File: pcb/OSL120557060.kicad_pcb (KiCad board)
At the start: 2 copper layers, 115.6 x 105.4 mm, 79 parts, among them J1 USB_B_Micro, J2 USB_B_Micro, J3 AVR-ISP-6, SW1 SW_SPST, SW10 SW_SPST, SW11 SW_SPST, SW12 SW_SPST, SW13 SW_SPST, SW14 SW_SPST, SW15 SW_SPST, SW16 SW_SPST, SW17 SW_SPST, SW18 SW_SPST, SW19 SW_SPST, SW2 SW_SPST, SW20 SW_SPST, SW21 SW_SPST, SW22 SW_SPST, SW23 SW_SPST, SW24 SW_SPST, SW25 SW_SPST, SW26 SW_SPST, SW27 SW_SPST, SW28 SW_SPST, SW29 SW_SPST, SW3 SW_SPST, SW30 SW_SPST, SW4 SW_SPST, SW5 SW_SPST, SW6 SW_SPST, SW7 SW_SPST, SW8 SW_SPST, SW9 SW_SPST, U1 ATmega328-PU, X1 16MHz

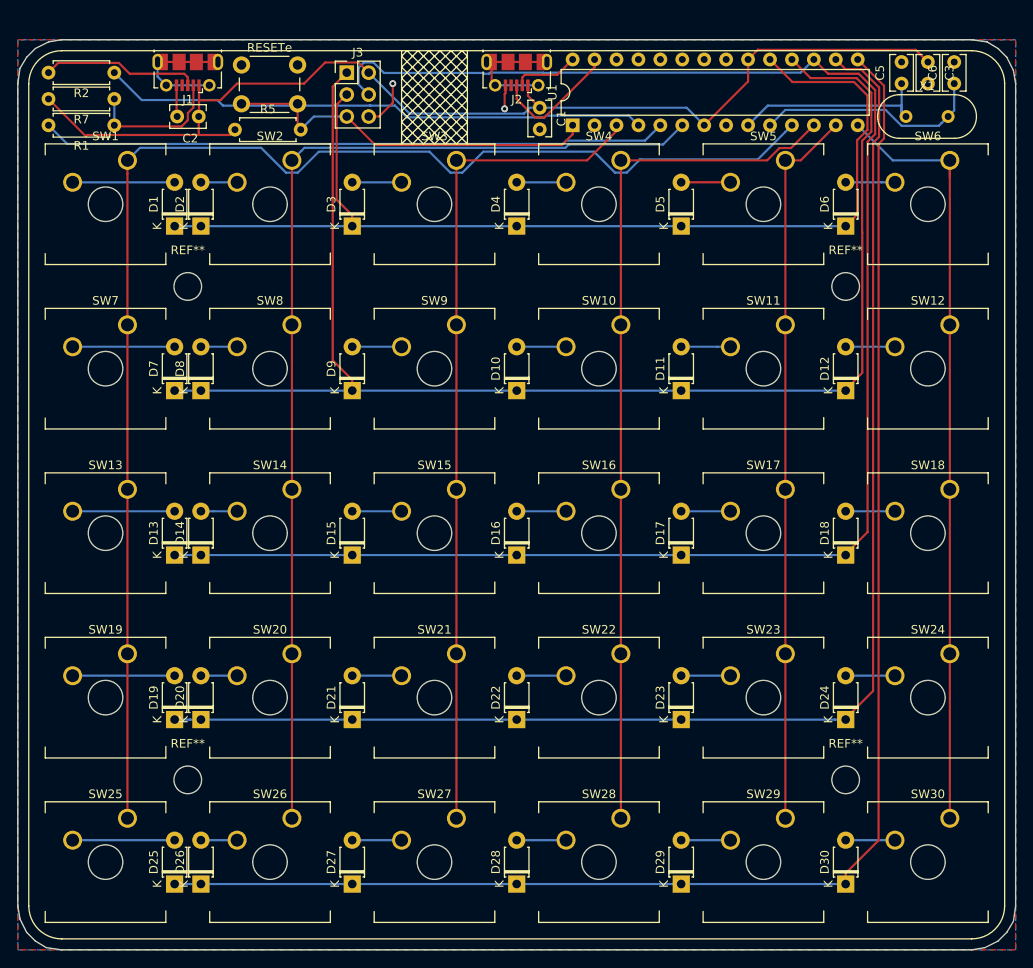
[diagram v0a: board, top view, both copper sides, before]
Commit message: added missing reset switch
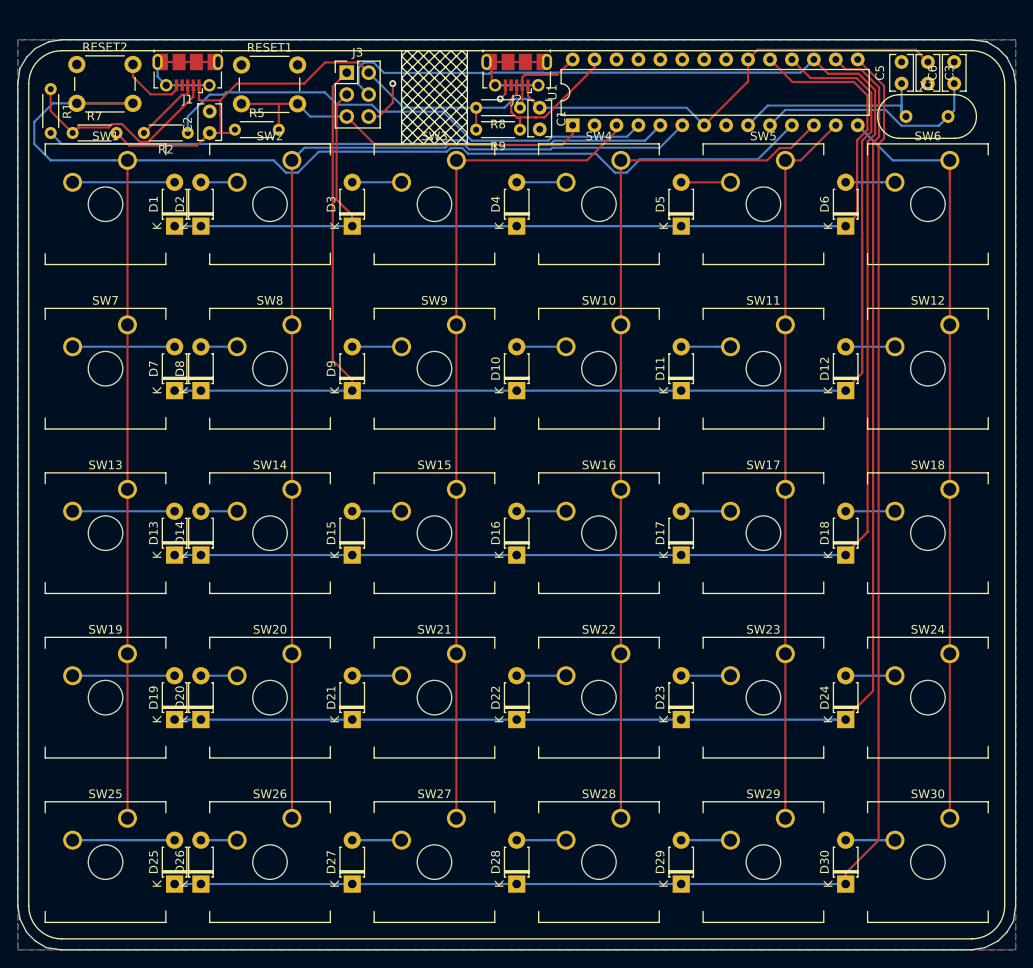
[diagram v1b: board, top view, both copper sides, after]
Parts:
- removed REF** (x4): MountingHole_3.2mm_M3, MountingHole:MountingHole_3.2mm_M3
- added R8: 10k, Resistor_THT:R_Axial_DIN0204_L3.6mm_D1.6mm_P5.08mm_Horizontal, F.Cu at (106.4, 58.7)
- added R9: 10k, Resistor_THT:R_Axial_DIN0204_L3.6mm_D1.6mm_P5.08mm_Horizontal, F.Cu at (106.4, 61.2)
- added RESET2: SW_SPST, Button_Switch_THT:SW_PUSH_6mm_H4.3mm, F.Cu at (55.1, 53.7)
- R1, R2, R5, R7: footprint Resistor_THT:R_Axial_DIN0207_L6.3mm_D2.5mm_P7.62mm_Horizontal -> Resistor_THT:R_Axial_DIN0204_L3.6mm_D1.6mm_P5.08mm_Horizontal
- moved R2 11.0 mm to (67.9, 61.6)
- moved R1 8.47 mm to (52.1, 56.5), turned to 270 degrees
- moved R7 6.23 mm to (54.6, 61.6), turned to 0 degrees
- moved C2 2.29 mm to (70.5, 61.6), turned to 90 degrees
- renumbered RESETe to RESET1
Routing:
- net /Col1: track 161.3 -> 191.3 mm
- net Net-(J1-Pad3): track 18.2 -> 8.00 mm
- net Net-(J1-Pad2): track 16.4 -> 24.9 mm
- net +5V: track 128.1 -> 122.1 mm
- net /USB_D+: track 63.5 -> 58.4 mm
- net GND: track 12.1 -> 15.5 mm
- net /SDA: track 14.8 -> 18.2 mm
- net /SCL: track 7.61 -> 10.3 mm
- net /Col2: track 123.1 -> 123.6 mm

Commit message: added smaller reset switches moved components to allow for all around plate
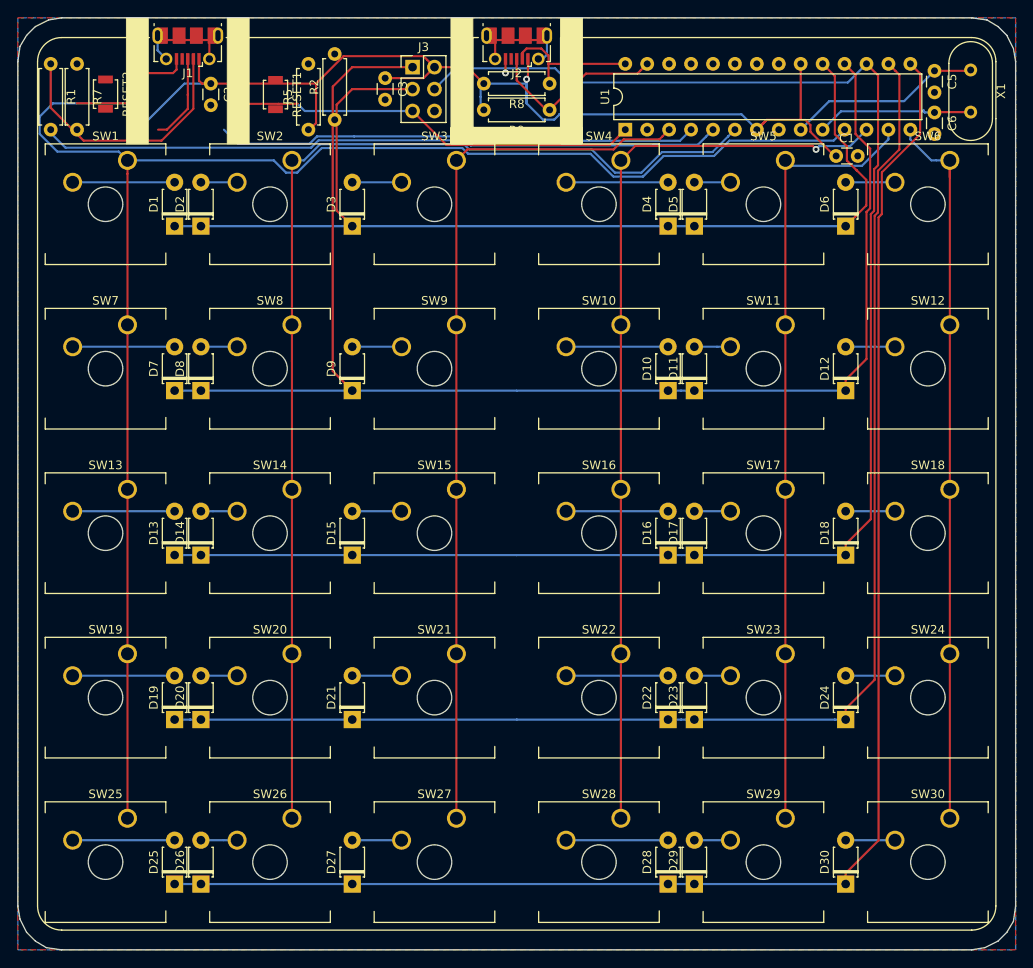
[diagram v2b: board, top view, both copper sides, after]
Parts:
- C1, C2, C3, C5, C6: footprint Capacitor_THT:C_Rect_L4.0mm_W2.5mm_P2.50mm -> Capacitor_THT:C_Disc_D3.0mm_W1.6mm_P2.50mm
- R1, R2, R5, R7, R8, R9: footprint Resistor_THT:R_Axial_DIN0204_L3.6mm_D1.6mm_P5.08mm_Horizontal -> Resistor_THT:R_Axial_DIN0207_L6.3mm_D2.5mm_P7.62mm_Horizontal
- RESET1, RESET2: footprint Button_Switch_THT:SW_PUSH_6mm_H4.3mm -> Button_Switch_SMD:SW_SPST_B3U-1000P
- moved C3 62.9 mm to (90.8, 55.2)
- moved C1 34.8 mm to (143.0, 64.3), turned to 0 degrees
- moved D10 17.5 mm to (123.6, 91.4)
- moved D16 17.5 mm to (123.6, 110.5)
- moved D22 17.5 mm to (123.6, 129.5)
- moved D28 17.5 mm to (123.6, 148.6)
- moved D4 17.5 mm to (123.6, 72.4)
- moved R2 17.1 mm to (85.0, 60.1), turned to 90 degrees
- moved X1 9.23 mm to (158.6, 54.3), turned to 270 degrees
- moved R5 8.51 mm to (81.9, 61.2), turned to 90 degrees
- moved R7 8.02 mm to (55.1, 53.6), turned to 270 degrees
- moved J3 7.65 mm to (94.0, 54.0)
- moved U1 6.12 mm to (118.6, 61.2)
- moved C2 5.72 mm to (70.6, 55.9), turned to 270 degrees
- moved RESET1 5.22 mm to (78.1, 57.1), turned to 270 degrees
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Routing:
- net /Row3: track 199.4 -> 189.3 mm
- net /Col2: track 123.6 -> 131.7 mm
- net /Xtal2: track 26.7 -> 18.6 mm
- net /Col5: track 83.7 -> 90.8 mm
- net GND: track 15.5 -> 8.48 mm, vias 2 -> 1
- net +5V: track 122.1 -> 128.7 mm, vias 0 -> 1
- net /USB_D-: track 72.5 -> 78.8 mm
- net /Col4: track 100.2 -> 106.5 mm, vias 0 -> 1
- net /SCL: track 10.3 -> 16.5 mm
- net Net-(D4-Pad2): track 5.72 -> 11.8 mm
- net Net-(D28-Pad2): track 5.72 -> 11.8 mm
- net Net-(D22-Pad2): track 5.72 -> 11.8 mm
- net Net-(D16-Pad2): track 5.72 -> 11.8 mm
- net Net-(D10-Pad2): track 5.72 -> 11.8 mm
- net /Reset: track 44.9 -> 50.7 mm
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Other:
- board size 115.6 x 105.4 mm -> 115.6 x 108 mm

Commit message: * added missing zener diodes on the usb port
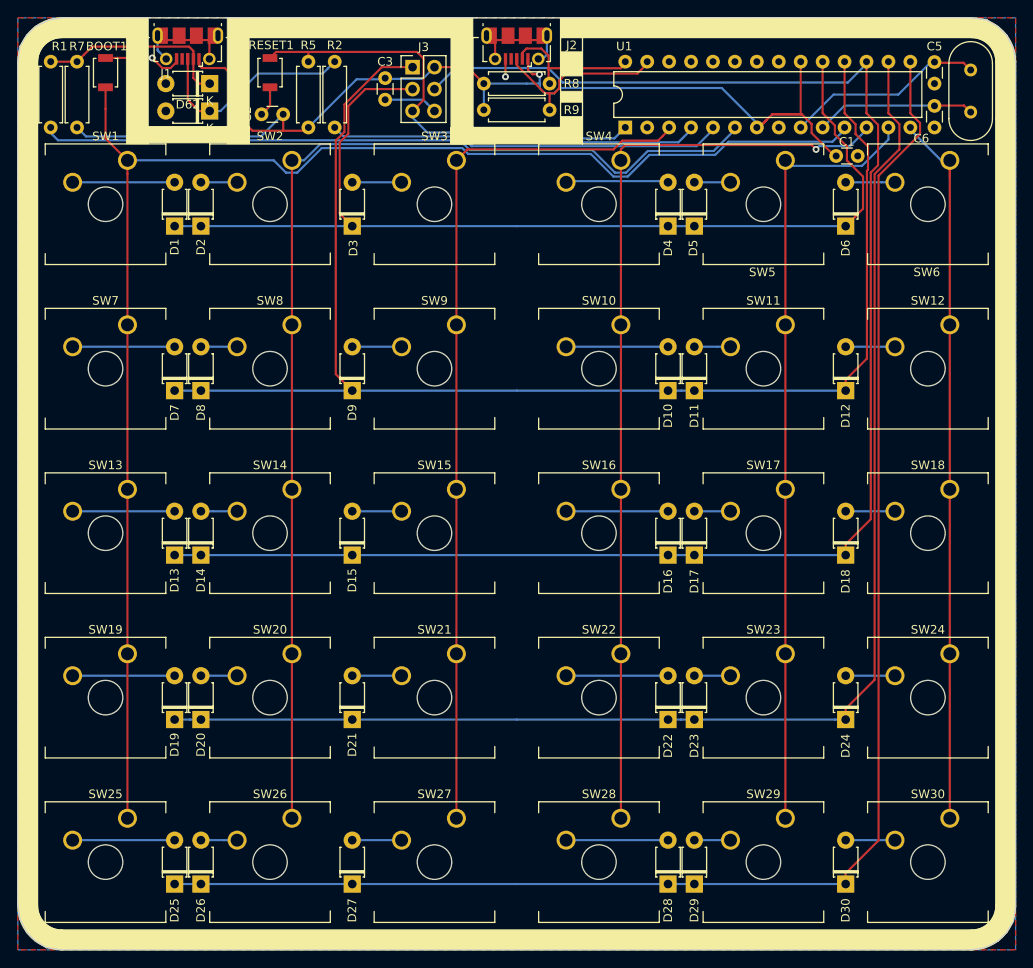
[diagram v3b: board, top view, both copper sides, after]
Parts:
- added D61: 3V6, Diode_THT:D_T-1_P5.08mm_Horizontal, F.Cu at (70.5, 59.1)
- added D62: 3V6, Diode_THT:D_T-1_P5.08mm_Horizontal, F.Cu at (70.5, 55.9)
- moved C2 9.11 mm to (79.0, 59.4), turned to 180 degrees
- moved RESET1 2.62 mm to (77.5, 54.6), turned to 90 degrees
- moved BOOT1 2.49 mm to (58.4, 54.6)
- moved C5 1.02 mm to (154.4, 53.4)
- moved R2 0.89 mm to (85.0, 61.0)
- moved C6 0.76 mm to (154.4, 58.5)
- moved R1 0.25 mm to (52.1, 53.3)
- moved R5 0.25 mm to (81.9, 61.0)
- moved R7 0.25 mm to (55.1, 53.3)
- moved U1 0.25 mm to (118.6, 61.0)
- renumbered RESET2 to BOOT1
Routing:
- net /Col1: track 196.0 -> 174.2 mm
- net Net-(D61-Pad1): track 9.70 -> 24.7 mm
- net /USB_D+: track 55.9 -> 42.6 mm
- net GND: track 8.48 -> 21.2 mm, vias 1 -> 2
- net +5V: track 128.7 -> 136.6 mm
- net Net-(D62-Pad1): track 30.0 -> 23.5 mm
- net /Reset: track 50.7 -> 53.3 mm
- net /Row2: track 164.3 -> 161.8 mm
- net /Row1: track 124.3 -> 122.8 mm
- net /Xtal1: track 22.5 -> 23.5 mm
- net /Col4: track 106.5 -> 107.3 mm
- net /Col6: track 84.9 -> 84.2 mm
- net /USB_D-: track 78.8 -> 78.1 mm

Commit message: moved from micro usb to usb-c (yw wilba)
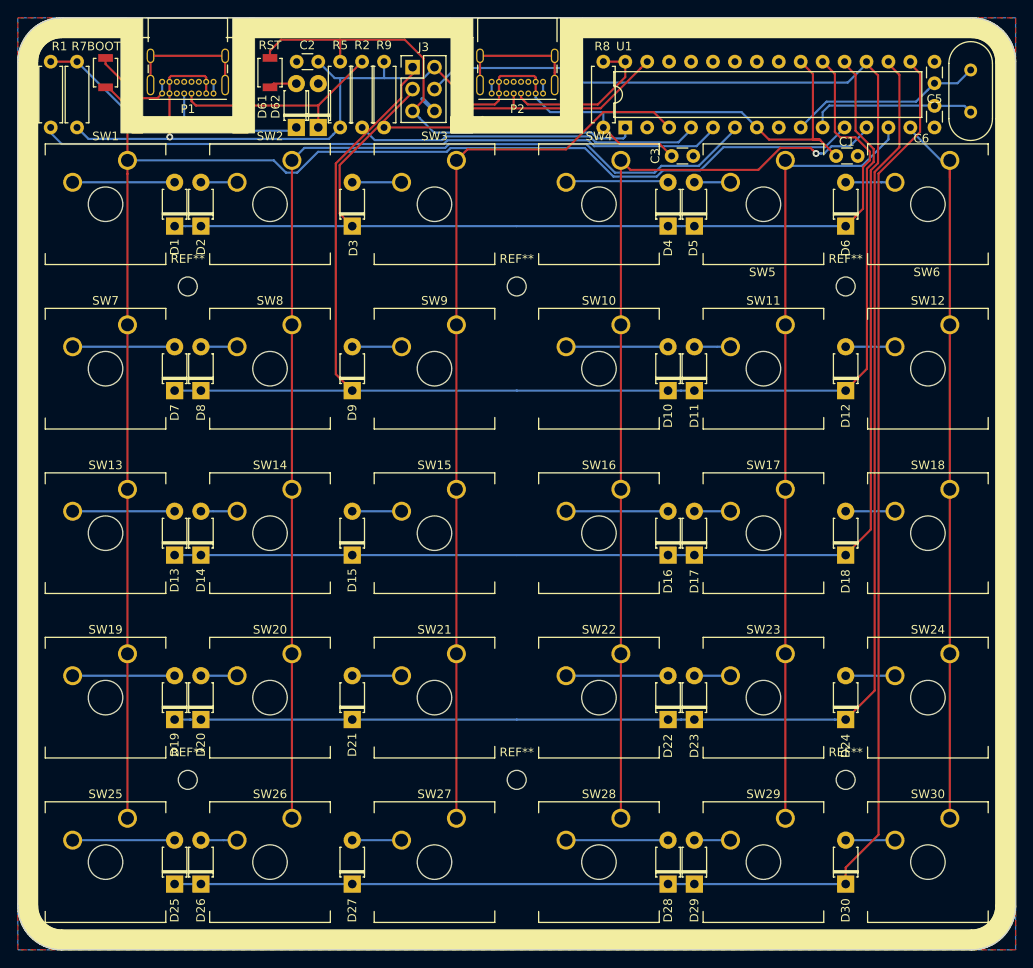
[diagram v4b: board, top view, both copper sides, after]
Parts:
- removed J1, J2: USB_B_Micro, Connector_USB:USB_Micro-B_Molex-105017-0001
- added P1: USB_C_Plug_USB2.0, Connector_USB:USB_C_Receptacle_GCT_USB4085, F.Cu at (70.9, 57.0)
- added P2: USB_C_Plug_USB2.0, Connector_USB:USB_C_Receptacle_GCT_USB4085, F.Cu at (109.1, 57.0)
- added REF**: MountingHole_2.2mm_M2, MountingHole:MountingHole_2.2mm_M2, F.Cu at (106.0, 79.4)
- added REF**: MountingHole_2.2mm_M2, MountingHole:MountingHole_2.2mm_M2, F.Cu at (106.0, 136.5)
- added REF**: MountingHole_2.2mm_M2, MountingHole:MountingHole_2.2mm_M2, F.Cu at (67.9, 136.5)
- added REF**: MountingHole_2.2mm_M2, MountingHole:MountingHole_2.2mm_M2, F.Cu at (67.9, 79.4)
- added REF**: MountingHole_2.2mm_M2, MountingHole:MountingHole_2.2mm_M2, F.Cu at (144.1, 79.4)
- added REF**: MountingHole_2.2mm_M2, MountingHole:MountingHole_2.2mm_M2, F.Cu at (144.1, 136.5)
- moved C3 34.4 mm to (124.0, 64.3), turned to 0 degrees
- moved R9 19.3 mm to (90.7, 61.0), turned to 90 degrees
- moved D61 12.7 mm to (83.1, 61.0), turned to 90 degrees
- moved D62 11.2 mm to (80.5, 61.0), turned to 90 degrees
- moved C2 7.33 mm to (83.1, 53.3)
- moved R8 6.72 mm to (116.1, 53.3), turned to 270 degrees
- moved R5 3.68 mm to (85.6, 61.0)
- moved R2 3.18 mm to (88.1, 61.0)
- moved C5 2.46 mm to (154.4, 55.8), turned to 90 degrees
- renumbered RESET1 to RST
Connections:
- net /Xtal1 renamed /Xtal_N
- net /Xtal2 renamed /Xtal_P
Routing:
- net Net-(P1-PadS1): track 0.00 -> 15.4 mm
- net Net-(P2-PadS1): track 0.00 -> 15.4 mm
- net /SDA: track 20.5 -> 35.4 mm
- net Net-(D62-Pad1): track 23.5 -> 36.4 mm
- net Net-(J1-Pad6): track 12.0 -> 0.00 mm
- net Net-(J2-Pad6): track 11.9 -> 0.00 mm
- net +5V: track 136.6 -> 146.6 mm
- net /Reset: track 53.3 -> 56.6 mm
- net /USB_D+: track 42.6 -> 39.8 mm
- net /SCL: track 16.9 -> 18.5 mm
- net /Col3: track 102.3 -> 103.9 mm
- net /Row2: track 161.8 -> 160.2 mm
- net GND: track 21.2 -> 19.7 mm, vias 2 -> 0
- net /Row1: track 122.8 -> 121.5 mm
- net /Xtal_P: track 18.8 -> 19.8 mm
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- added copper zone on F.Cu, net Net-(P2-PadB5)
- removed copper zone on F.Cu, net (none)
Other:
- outline, holes or cut-outs redrawn

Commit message: * added mount pis to pcb * improved plate layout
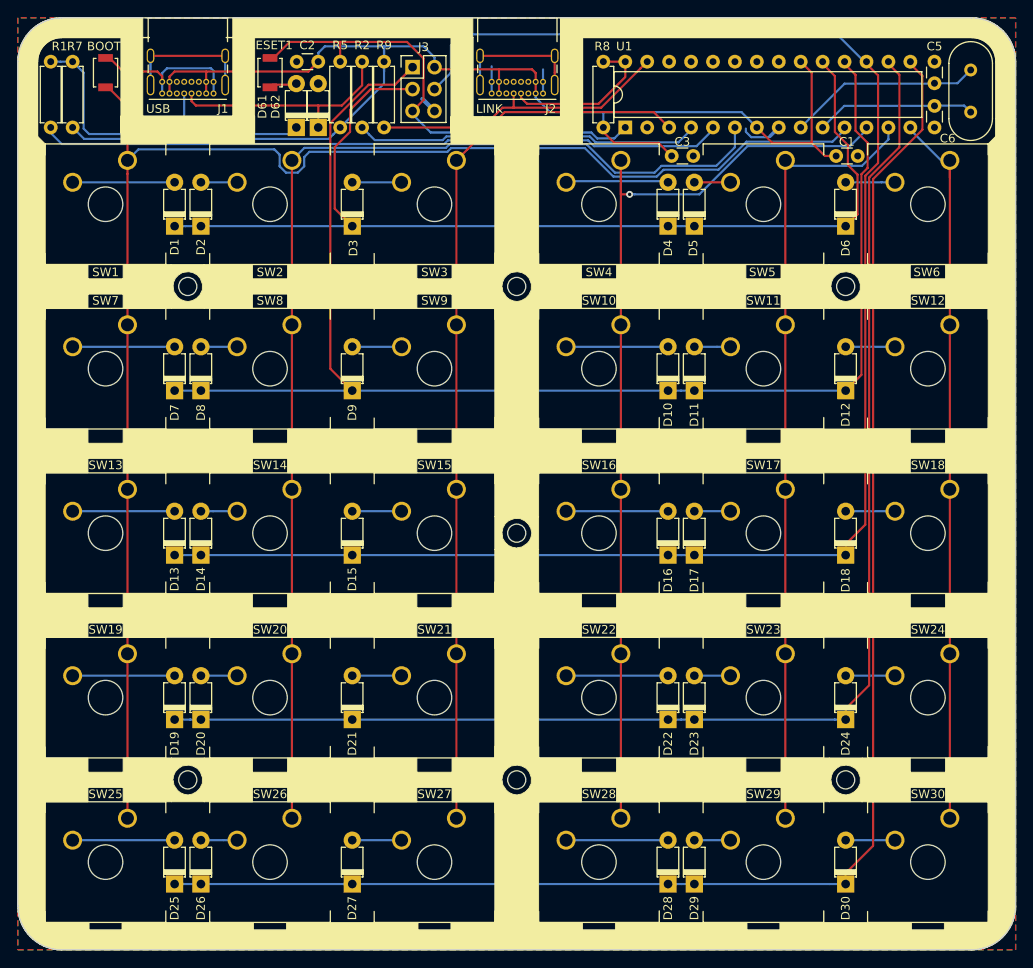
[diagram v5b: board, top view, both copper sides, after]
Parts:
- removed the REF** at (106.0, 79.4)
- removed the REF** at (106.0, 136.5)
- removed the REF** at (67.9, 136.5)
- removed the REF** at (67.9, 79.4)
- removed the REF** at (144.1, 79.4)
- removed the REF** at (144.1, 136.5)
- added REF**: MountingHole_2.1mm, MountingHole:MountingHole_2.1mm, F.Cu at (106.0, 79.4)
- added REF**: MountingHole_2.1mm, MountingHole:MountingHole_2.1mm, F.Cu at (106.0, 108.0)
- added REF**: MountingHole_2.1mm, MountingHole:MountingHole_2.1mm, F.Cu at (144.1, 136.5)
- added REF**: MountingHole_2.1mm, MountingHole:MountingHole_2.1mm, F.Cu at (144.1, 79.4)
- added REF**: MountingHole_2.1mm, MountingHole:MountingHole_2.1mm, F.Cu at (106.0, 136.5)
- added REF**: MountingHole_2.1mm, MountingHole:MountingHole_2.1mm, F.Cu at (67.9, 136.5)
- added REF**: MountingHole_2.1mm, MountingHole:MountingHole_2.1mm, F.Cu at (67.9, 79.4)
- moved R7 0.51 mm to (54.6, 53.3)
- renumbered P1 to J1, P2 to J2, RST to RESET1
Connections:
- J2 pad B5: Net-(P2-PadB5) -> (no net)
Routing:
- net GND: track 19.7 -> 36.9 mm
- net +5V: track 146.6 -> 161.8 mm, vias 1 -> 0
- net Net-(D62-Pad1): track 36.4 -> 40.5 mm
- net /Col4: track 107.6 -> 111.7 mm
- net /Row3: track 189.4 -> 192.7 mm
- net /Col1: track 174.3 -> 176.8 mm
- net /Row2: track 160.2 -> 162.0 mm
- net Net-(D61-Pad1): track 25.5 -> 27.1 mm
- net /Reset: track 56.6 -> 55.2 mm
- net /Col2: track 131.7 -> 132.9 mm
- net /Xtal_P: track 19.8 -> 18.8 mm
- net /Row1: track 121.5 -> 122.4 mm
- added copper zone on F.Cu, net (none)
- removed copper zone on F.Cu, net Net-(P2-PadB5)
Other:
- board text added: "LINK"
- board text added: "USB"
